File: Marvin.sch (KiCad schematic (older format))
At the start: 11 parts, among them M1 Motor_DC, M2 Stepper_Motor_bipolar, M3 Stepper_Motor_bipolar, U1 L7805, U2 L298HN, U3 DM420, U4 DM420

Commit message: Exchanged Arduino Uno to Arduino Mega 2560 and added SD Card Module
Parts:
- removed A1: Arduino_UNO_R3, Modules:Arduino_UNO_R3_WithMountingHoles, symbol MCU_Module:Arduino_UNO_R3
- removed U2: L298HN, Package_TO_SOT_THT:TO-220-15_P2.54x2.54mm_StaggerOdd_Lead4.58mm_Vertical, symbol Driver_Motor:L298HN
- added J?: Arduino_Mega_Header, symbol w_connectors:Arduino_Mega_Header
- added U?: ADAFRUIT254, symbol Marvin:ADAFRUIT254
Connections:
- net labels added: CLK, MISO, MOSI
- wire segments 84 -> 83
- no-connect marks 26 -> 4
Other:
- note removed: "DC Motordriver Shield"
- note removed: "L298 Motorr Driver Shield\n1A - 36 V max.\n"

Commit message: Limit Switches und Rotary Encoders hinzugefuegt.
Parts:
- added R? (x2): R, symbol Device:R
- added SW?: Rotary_Encoder, symbol Device:Rotary_Encoder
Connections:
- net +5VD: now also R?.1, R?.1
- net B: now reaches J?.63 (RXD2/19)
- net B: now also SW?.B
- net A: now reaches J?.64 (TXD2/18)
- net A: now also SW?.A
- net LIM2: now reaches J?.72 (PWM3/3)
- net LIM2: now also R?.2
- net LIM1: now reaches J?.73 (SS1/PWM4/SD-CS/4)
- net LIM1: now also R?.2
- no-connect marks 4 -> 2
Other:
- note added: "Polierspindel mit Drehzahl-\nmessung. DC Motor und \nRotary Encoder"
- note added: "SD Card Modul"
- note added: "SD Card Modul von Adafruit\nAdafruit 254\n"
- moved on the sheet: D1, M1
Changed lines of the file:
@@
 L motors:Motor_DC M1
 U 1 1 5BE07F6E
-P 1450 6250
-F 0 "M1" H 1550 6350 50  0000 L CNN
-F 1 "Motor_DC" H 1550 6050 50  0000 L TNN
-F 2 "TerminalBlocks_Phoenix:TerminalBlock_Phoenix_MKDS1.5-2pol" H 1450 6160 50  0001 C CNN
-F 3 "" H 1450 6160 50  0001 C CNN
-	1    1450 6250
+P 1100 4200
+F 0 "M1" H 1200 4300 50  0000 L CNN
+F 1 "Motor_DC" H 1200 4000 50  0000 L TNN
+F 2 "TerminalBlocks_Phoenix:TerminalBlock_Phoenix_MKDS1.5-2pol" H 1100 4110 50  0001 C CNN
+F 3 "" H 1100 4110 50  0001 C CNN
+	1    1100 4200
 	1    0    0    -1
 $EndComp
@@
 L Diode:1N4001 D1
 U 1 1 5BE093C6
-P 2200 6250
-F 0 "D1" H 2200 6350 50  0000 C CNN
-F 1 "1N4001" H 2200 6150 50  0000 C CNN
-F 2 "Diodes_THT:D_DO-41_SOD81_P2.54mm_Vertical_AnodeUp" H 2200 6075 50  0001 C CNN
-F 3 "" H 2200 6250 50  0001 C CNN
-	1    2200 6250
+P 1850 4200
+F 0 "D1" H 1850 4300 50  0000 C CNN
+F 1 "1N4001" H 1850 4100 50  0000 C CNN
+F 2 "Diodes_THT:D_DO-41_SOD81_P2.54mm_Vertical_AnodeUp" H 1850 4025 50  0001 C CNN
+F 3 "" H 1850 4200 50  0001 C CNN
+	1    1850 4200
 	0    1    1    0
 $EndComp
-Text GLabel 1450 5900 1    60   Input ~ 0
+Text GLabel 1100 3850 1    60   Input ~ 0
 OUT1
-Text GLabel 1450 6750 3    60   Input ~ 0
+Text GLabel 1100 4700 3    60   Input ~ 0
 OUT2
-Text Notes 1650 5700 0    79   ~ 16
+Text Notes 1550 3650 0    79   ~ 16
 Polierspindel\n
 Wire Wire Line
@@
 	8800 3650 8600 3650
 Wire Wire Line
-	1450 6550 1450 6600
-Wire Wire Line
-	1450 5900 1450 6000
-Wire Wire Line
-	2200 6100 2200 6000
-Wire Wire Line
-	2200 6000 1450 6000
-Connection ~ 1450 6000
-Wire Wire Line
-	1450 6600 2200 6600
-Wire Wire Line
-	2200 6600 2200 6400
-Connection ~ 1450 6600
+	1100 4500 1100 4550
+Wire Wire Line
+	1100 3850 1100 3950
+Wire Wire Line
+	1850 4050 1850 3950
+Wire Wire Line
+	1850 3950 1100 3950
+Connection ~ 1100 3950
+Wire Wire Line
+	1100 4550 1850 4550
+Wire Wire Line
+	1850 4550 1850 4350
+Connection ~ 1100 4550
 Text Notes 2950 700  0    79   ~ 16
 5V Stromversorgung
@@
 	8700 2800 8800 2800
 Wire Wire Line
-	1450 6000 1450 6050
-Wire Wire Line
-	1450 6600 1450 6750
+	1100 3950 1100 4000
+Wire Wire Line
+	1100 4550 1100 4700
 $Comp
 L power:PWR_FLAG #FLG0101
@@
 Wire Wire Line
 	1700 1450 1700 1600
-NoConn ~ 5650 1950
-NoConn ~ 5600 2000
-NoConn ~ 5650 2050
 Wire Wire Line
 	5400 2250 5650 2250
@@
 Wire Wire Line
 	6800 4150 6650 4150
+Text Notes 1850 2400 0    79   ~ 16
+SD Card Modul
+Text Notes 1850 2600 0    59   ~ 0
+SD Card Modul von Adafruit\nAdafruit 254\n
+$Comp
+L Device:R R?
+U 1 1 5BF0624E
+P 7350 2500
+F 0 "R?" H 7420 2546 50  0000 L CNN
+F 1 "R" H 7420 2455 50  0000 L CNN
+F 2 "" V 7280 2500 50  0001 C CNN
+F 3 "~" H 7350 2500 50  0001 C CNN
+	1    7350 2500
+	1    0    0    -1
+$EndComp
+$Comp
+L Device:R R?
+U 1 1 5BF062C0
+P 7600 2550
+F 0 "R?" H 7670 2596 50  0000 L CNN
+F 1 "R" H 7670 2505 50  0000 L CNN
+F 2 "" V 7530 2550 50  0001 C CNN
+F 3 "~" H 7600 2550 50  0001 C CNN
+	1    7600 2550
+	1    0    0    -1
+$EndComp
+$Comp
+L power:+5VD #PWR?
+U 1 1 5BF063E1
+P 7350 2250
+F 0 "#PWR?" H 7350 2100 50  0001 C CNN
+F 1 "+5VD" H 7350 2390 50  0000 C CNN
+F 2 "" H 7350 2250 50  0001 C CNN
+F 3 "" H 7350 2250 50  0001 C CNN
+	1    7350 2250
+	1    0    0    -1
+$EndComp
+$Comp
+L power:+5VD #PWR?
+U 1 1 5BF06454
+P 7600 2300
+F 0 "#PWR?" H 7600 2150 50  0001 C CNN
+F 1 "+5VD" H 7600 2440 50  0000 C CNN
+F 2 "" H 7600 2300 50  0001 C CNN
+F 3 "" H 7600 2300 50  0001 C CNN
+	1    7600 2300
+	1    0    0    -1
+$EndComp
+Wire Wire Line
+	7350 2250 7350 2350
+Wire Wire Line
+	7600 2300 7600 2400
+Wire Wire Line
+	6650 2650 7350 2650
+Wire Wire Line
+	6700 2700 7600 2700
+Text GLabel 7350 2900 3    50   Input ~ 0
+LIM1
+Text GLabel 7600 2900 3    50   Input ~ 0
+LIM2
+Wire Wire Line
+	7350 2650 7350 2900
+Connection ~ 7350 2650
+Wire Wire Line
+	7600 2700 7600 2900
+Connection ~ 7600 2700
+$Comp
+L Device:Rotary_Encoder SW?
+U 1 1 5BF4D015
+P 1250 5600
+F 0 "SW?" H 1195 5233 50  0000 C CNN
+F 1 "Rotary_Encoder" H 1195 5324 50  0000 C CNN
+F 2 "" H 1100 5760 50  0001 C CNN
+F 3 "~" H 1250 5860 50  0001 C CNN
+	1    1250 5600
+	-1   0    0    1
+$EndComp
+NoConn ~ 1550 5600
+Wire Wire Line
+	6650 3200 6750 3200
+Wire Wire Line
+	6750 3200 6750 3250
+Text GLabel 6800 3150 2    50   Input ~ 0
+A
+Text GLabel 6800 3250 2    50   Input ~ 0
+B
+Wire Wire Line
+	6750 3250 6800 3250
+Wire Wire Line
+	6800 3150 6700 3150
+Text GLabel 1700 5700 2    50   Input ~ 0
+A
+Text GLabel 1700 5500 2    50   Input ~ 0
+B
+Wire Wire Line
+	1700 5700 1550 5700
+Wire Wire Line
+	1700 5500 1550 5500
+Text Notes 2050 3950 0    59   ~ 0
+Polierspindel mit Drehzahl-\nmessung. DC Motor und \nRotary Encoder
 $EndSCHEMATC

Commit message: Added MC Description in Schematic
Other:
- note added: "AVR Atmega2560 - 16 MHz"
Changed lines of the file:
@@
 Text Notes 2050 3950 0    59   ~ 0
 Polierspindel mit Drehzahl-\nmessung. DC Motor und \nRotary Encoder
+Text Notes 5450 4450 0    59   ~ 0
+AVR Atmega2560 - 16 MHz
 $EndSCHEMATC

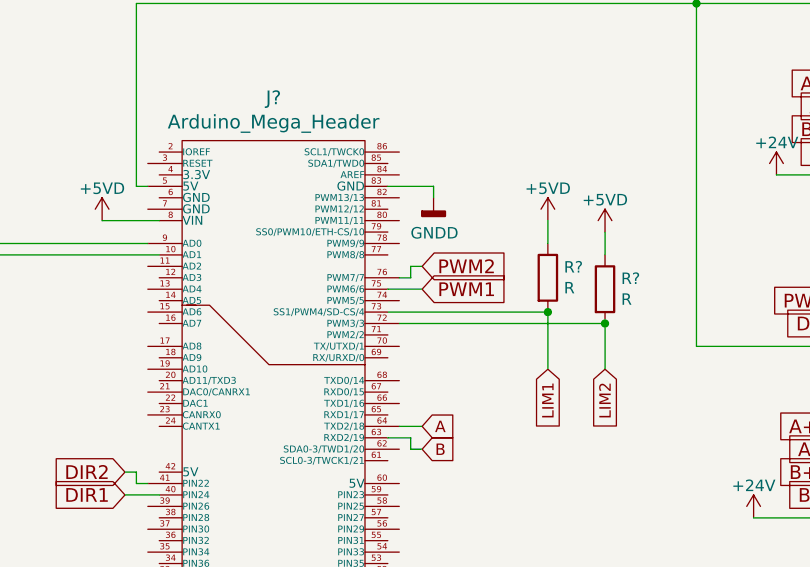
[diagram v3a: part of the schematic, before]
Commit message: Updatet PWM Outputs matching Timer 3 and 4
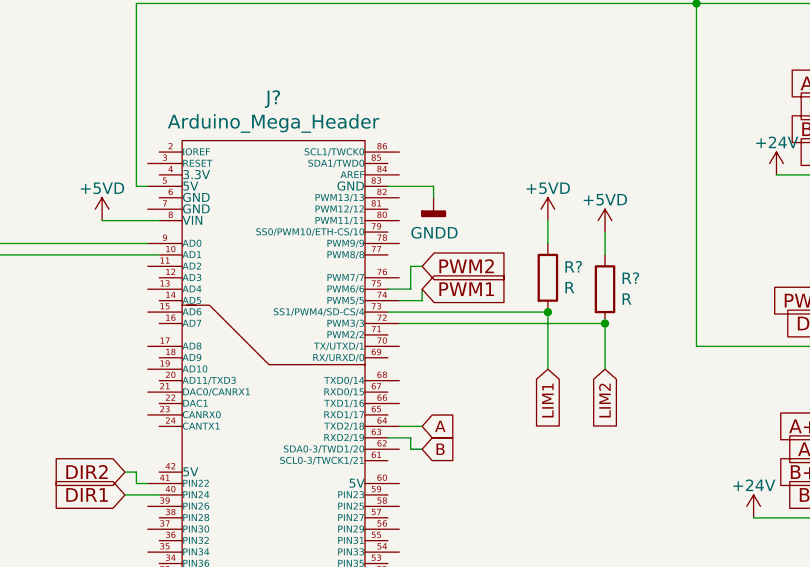
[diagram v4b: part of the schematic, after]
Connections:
- net PWM1: now also J?.74 (PWM5/5); no longer J?.75 (PWM6/6)
- net PWM2: now also J?.75 (PWM6/6); no longer J?.76 (PWM7/7)
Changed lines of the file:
@@
 $EndComp
-Wire Wire Line
-	6850 2150 6850 2100
-Wire Wire Line
-	6850 2100 6650 2100
 Wire Wire Line
 	5600 2100 5550 2100
@@
 Wire Wire Line
 	5550 1300 8000 1300
-Wire Wire Line
-	6800 2450 6750 2450
-Wire Wire Line
-	6750 2450 6750 2500
-Wire Wire Line
-	6750 2500 6700 2500
-Wire Wire Line
-	6800 2550 6650 2550
 Wire Wire Line
 	5500 3350 5550 3350
@@
 Text Notes 5450 4450 0    59   ~ 0
 AVR Atmega2560 - 16 MHz
+Wire Wire Line
+	6850 2100 6650 2100
+Wire Wire Line
+	6850 2150 6850 2100
+Wire Wire Line
+	6750 2450 6800 2450
+Wire Wire Line
+	6800 2600 6800 2550
+Wire Wire Line
+	6700 2600 6800 2600
+Wire Wire Line
+	6650 2550 6750 2550
+Wire Wire Line
+	6750 2550 6750 2450
 $EndSCHEMATC

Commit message: Kleine Aktualisierung
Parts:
- removed U?: ADAFRUIT254, symbol Marvin:ADAFRUIT254
- added D2: 1N4001, Diodes_THT:D_DO-41_SOD81_P2.54mm_Vertical_AnodeUp, symbol Marvin-rescue:1N4001-Diode
- added M4: Motor_DC, TerminalBlocks_Phoenix:TerminalBlock_Phoenix_MKDS1.5-2pol, symbol Marvin-rescue:Motor_DC-motors
- added U2: RoetzerRegler, symbol Marvin:RoetzerRegler
- added U5: Motortreiber, symbol Marvin:Motortreiber
- C1, C2: symbol Device:C -> Marvin-rescue:C-Device
- D1: symbol Diode:1N4001 -> Marvin-rescue:1N4001-Diode
- J1: renamed from J?; symbol w_connectors:Arduino_Mega_Header -> Marvin-rescue:Arduino_Mega_Header-w_connectors
- M1: symbol motors:Motor_DC -> Marvin-rescue:Motor_DC-motors
- M2, M3: symbol motors:Stepper_Motor_bipolar -> Marvin-rescue:Stepper_Motor_bipolar-motors
- R1, R2: renamed from R?; symbol Device:R -> Marvin-rescue:R-Device
- SW1: renamed from SW?; symbol Device:Rotary_Encoder -> Marvin-rescue:Rotary_Encoder-Device
- U1: symbol regul:L7805 -> Marvin-rescue:L7805-regul
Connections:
- net +24V: now also U2.~ (Vout), U5.~ (Vcc); no longer C1.1, U1.1 (IN)
- net +5VD: now also U5.~ (Vcc)
- net DIR1: now also U5.~ (Vcc)
- net DIR2: now also J1.59 (PIN23), U5.~ (Vcc); no longer J1.41 (PIN22)
- net GNDD: now also U2.~ (Vout), U5.~ (Vcc)
- net LIM1: no longer J1.73 (SS1/PWM4/SD-CS/4)
- net LIM2: no longer J1.72 (PWM3/3)
- net OUT1: now also U5.~ (Vcc)
- net OUT2: now also U5.~ (Vcc)
- net DIR3: now reaches J1.15 (AD6)
- net DIR3: now also U5.~ (Vcc)
- net DIR4: now reaches J1.16 (AD7)
- net DIR4: now also U5.~ (Vcc)
- net ENCODER_PIN: now reaches J1.62 (SDA0-3/TWD1/20)
- net ENCODER_PIN: now also SW1.C
- net RENC_A: now reaches J1.71 (PWM2/2)
- net RENC_A: now also SW1.A
- net PWM_PressurePump: now reaches J1.80 (PWM11/11)
- net PWM_PressurePump: now also U5.~ (Vcc)
- net A: no longer names the net of J1.64 (TXD2/18)
- net A: no longer SW1.A
- net B: no longer names the net of J1.63 (RXD2/19)
- net B: no longer SW1.B
- net CLK: no longer names the net of J1.26 (PIN52/AD14/RXD3)
- net MISO: no longer names the net of J1.27 (PIN50)
- net MOSI: no longer names the net of J1.45 (PIN51)
- new net +12V: C1.1, U1.1 (IN), U2.~ (Vout)
- new net GND: U2.~ (Vout)
- new net OUT3: D2.1 (K), M4.1 (+), U5.~ (Vcc)
- new net OUT4: D2.2 (A), M4.2 (-), U5.~ (Vcc)
- new net PWM3: U5.~ (Vcc)
- new net RENC_B: J1.72 (PWM3/3), SW1.B
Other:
- note added: "Polierpumpe\n"
- note removed: "1.5A - 5V fix max \n35 max Input Voltage\n\nHinweis: Nur zur Sicherheit. Der Arduino schafft \nnormalerweise von selber aus bis zu 24V"
- note removed: "SD Card Modul"
- note removed: "SD Card Modul von Adafruit\nAdafruit 254\n"
- moved on the sheet: C1, C2, SW1, U1

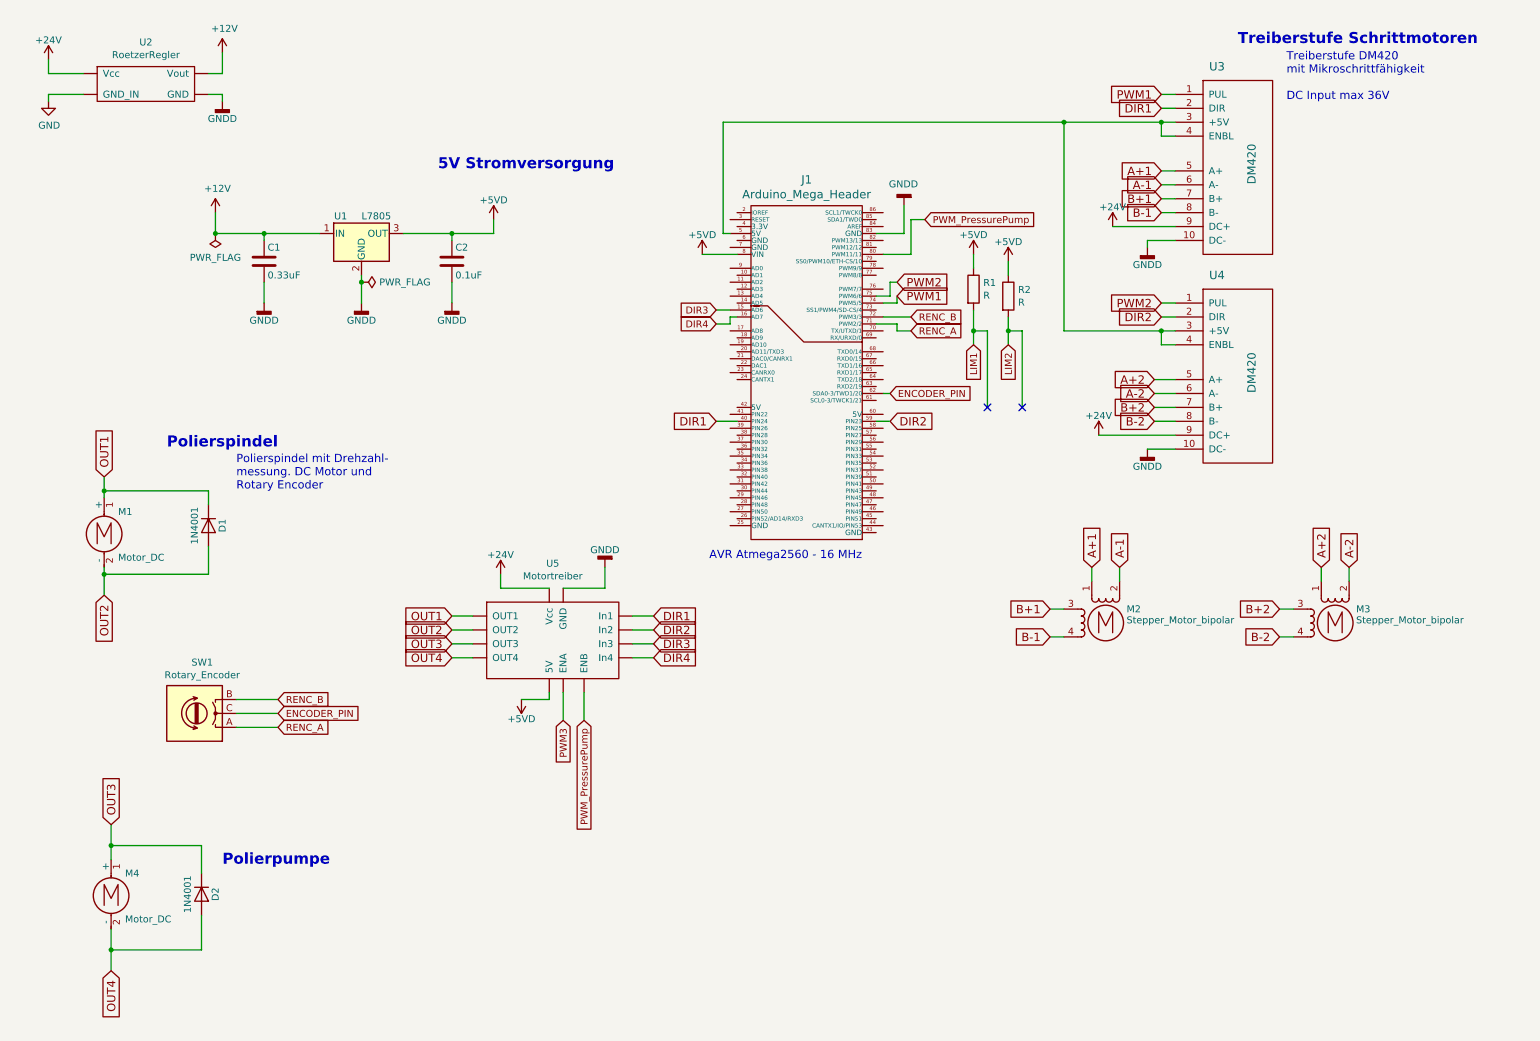
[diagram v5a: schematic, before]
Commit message: Aktualisierung Raspberry Pi und Zellen
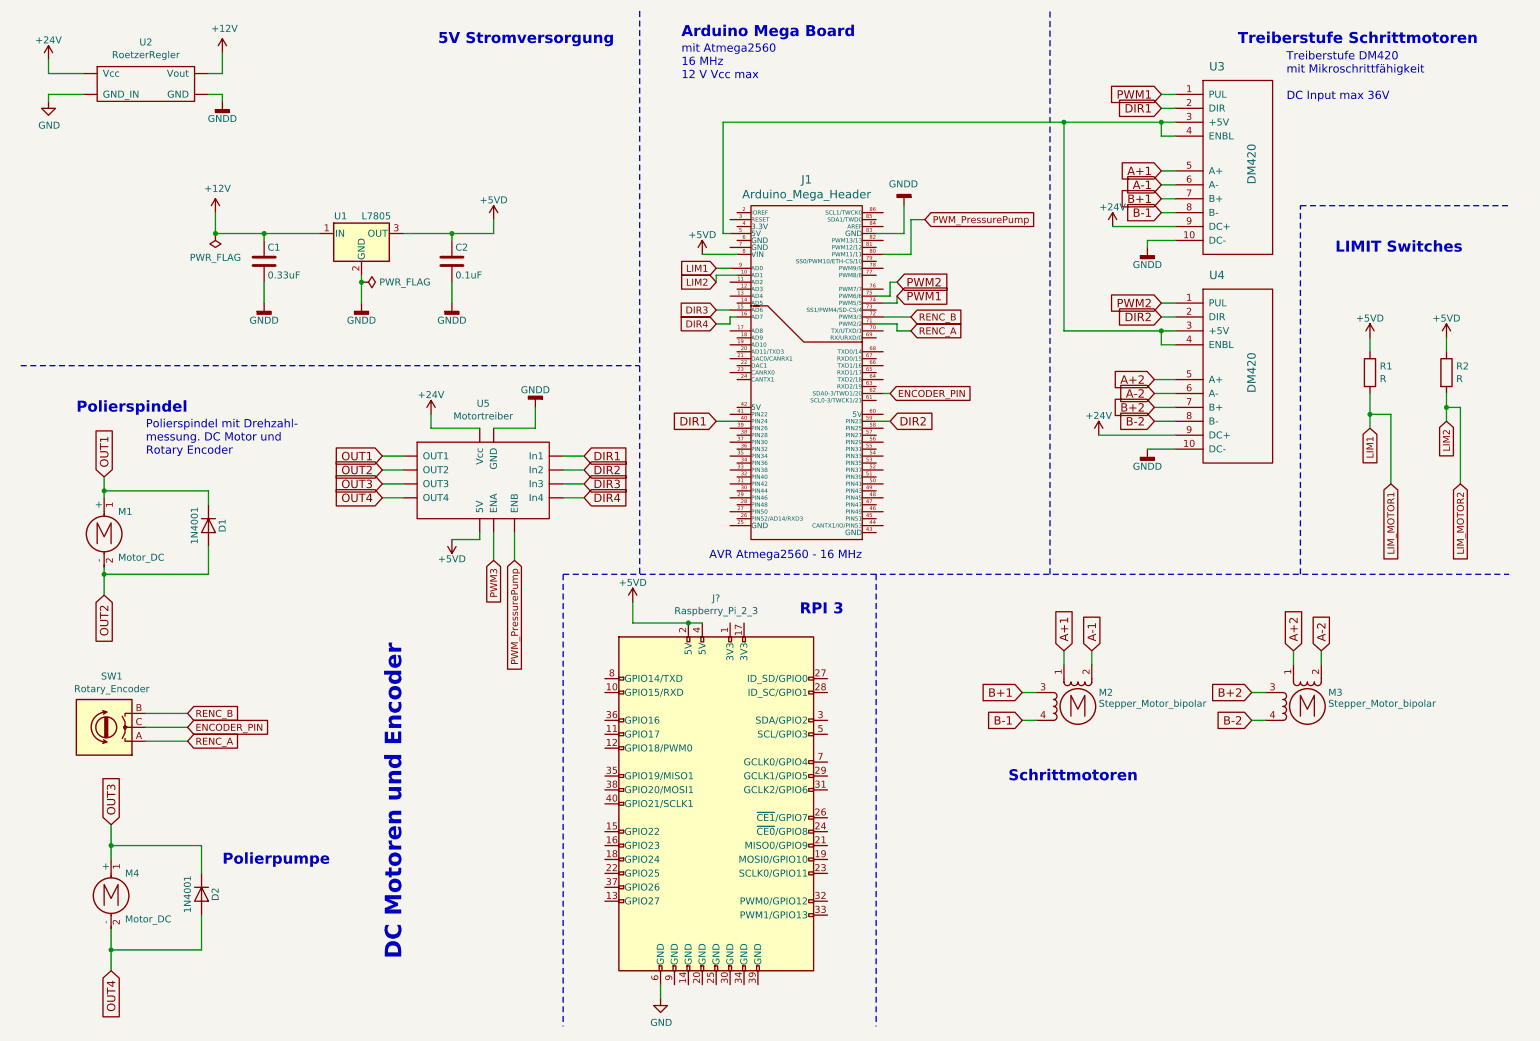
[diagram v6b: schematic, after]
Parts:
- added J?: Raspberry_Pi_2_3, symbol Connector:Raspberry_Pi_2_3
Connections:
- net +5VD: now also J?.2 (5V), J?.4 (5V)
- net GND: now also J?.6 (GND)
- net LIM1: now also J1.9 (AD0)
- net LIM2: now also J1.10 (AD1)
- no-connect marks 2 -> 0
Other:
- note added: "Arduino Mega Board"
- note added: "DC Motoren und Encoder\n"
- note added: "LIMIT Switches\n"
- note added: "RPI 3\n"
- note added: "Schrittmotoren\n"
- note added: "mit Atmega2560\n16 MHz\n12 V Vcc max"
- moved on the sheet: M2, M3, R1, R2, SW1, U5

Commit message: PWM 3 nachgetragen
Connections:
- net PWM3: now also J1.81 (PWM12/12)
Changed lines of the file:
@@
 Wire Wire Line
 	6850 1900 6850 2100
-Wire Wire Line
-	7000 2000 6900 2000
-Wire Wire Line
-	6900 2000 6900 2250
-Wire Wire Line
-	6900 2250 6700 2250
 Text GLabel 4050 4450 3    50   Input ~ 0
 PWM_PressurePump
@@
 Text Notes 3250 5050 3    118  ~ 24
 DC Motoren und Encoder\n
+Text GLabel 6750 2200 2    50   Input ~ 0
+PWM3
+Wire Wire Line
+	6650 2200 6750 2200
+Wire Wire Line
+	7000 2000 6900 2000
+Wire Wire Line
+	6750 2250 6750 2300
+Wire Wire Line
+	7100 2300 7100 2100
+Wire Wire Line
+	7100 2100 6900 2100
+Wire Wire Line
+	6900 2100 6900 2000
+Wire Wire Line
+	6750 2250 6700 2250
+Wire Wire Line
+	6750 2300 7100 2300
 $EndSCHEMATC
